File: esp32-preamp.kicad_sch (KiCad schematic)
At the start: 55 parts, among them J1 INPUT 1, J10 LFE, J11 OUT, J2 INPUT 2, J3 INPUT 3, J4 AMP PWR, J5 VOLUME, J6 TSOP382, J7 SELECT, J8 POT MOTOR, J9 PWR IN, Q1 2N3904, Q2 2N3904, Q3 2N3904, Q4 2N3904, U3 TSR0.5-2450, U4 TLV702475DBV, U5 TPS60402DBV, U6 ESP32 D1 Mini, U7 TPS72301DBV

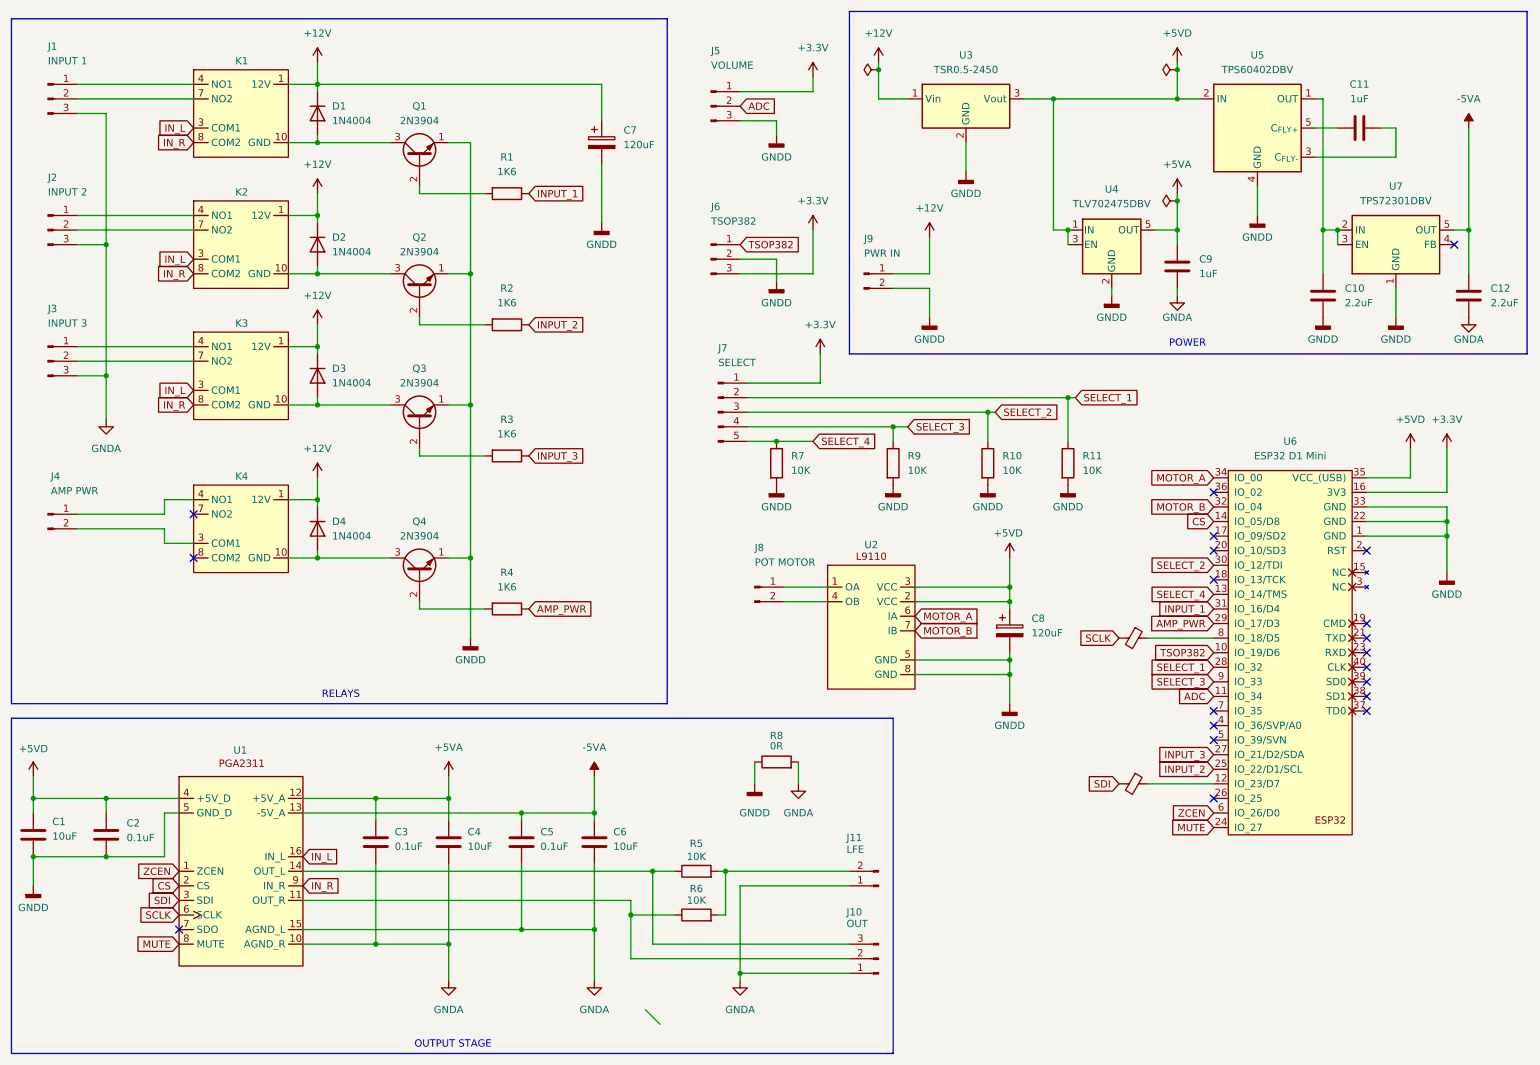
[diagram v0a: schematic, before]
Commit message: Fix J7 to reflect two input preamp
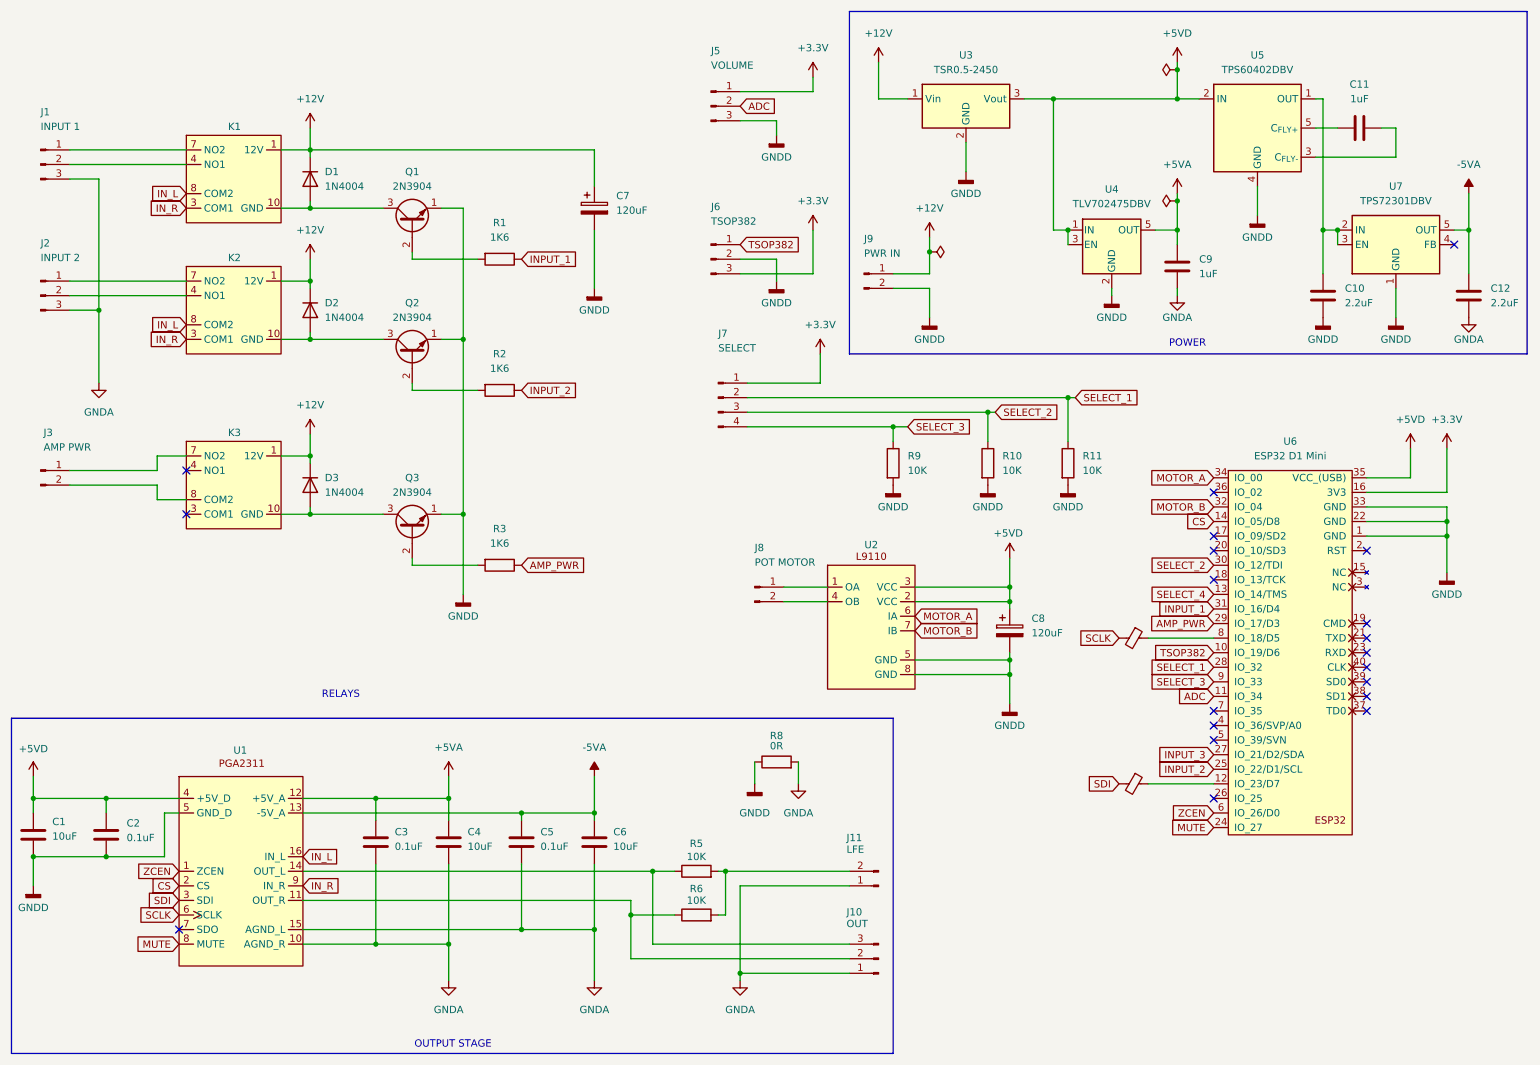
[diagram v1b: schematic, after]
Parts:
- removed D3: 1N4004, Diode_THT:D_DO-41_SOD81_P10.16mm_Horizontal, symbol Diode:1N4004
- removed J3: INPUT 3, Connector_JST:JST_XH_B3B-XH-A_1x03_P2.50mm_Vertical, symbol Connector:Conn_01x03_Pin
- removed J7: SELECT, Connector_JST:JST_XH_B5B-XH-A_1x05_P2.50mm_Vertical, symbol Connector:Conn_01x05_Pin
- removed K3: (no value), Panasonic TQ2:RELAY_TQ2_PAN, symbol Relay:TQ2
- removed Q3: 2N3904, Package_TO_SOT_THT:TO-92_Inline, symbol Transistor_BJT:2N3904
- removed R3: 1K6, Resistor_SMD:R_1206_3216Metric_Pad1.30x1.75mm_HandSolder, symbol Device:R
- removed R7: 10K, Resistor_SMD:R_1206_3216Metric_Pad1.30x1.75mm_HandSolder, symbol Device:R
- added J7: SELECT, Connector_JST:JST_XH_B4B-XH-A_1x04_P2.50mm_Vertical, symbol Connector:Conn_01x04_Pin
- C4: footprint Capacitor_SMD:C_1206_3216Metric_Pad1.33x1.80mm_HandSolder -> Capacitor_THT:C_Radial_D4.0mm_H5.0mm_P1.50mm
- R5, R6: footprint Resistor_THT:R_Axial_Power_L38.0mm_W9.0mm_P40.64mm -> Resistor_THT:R_Axial_Power_L30.0mm_W9.0mm_P36.4mm
- U4: footprint Package_TO_SOT_SMD:SOT-23-5_HandSoldering -> Package_TO_SOT_SMD:SOT-23-5
- U6: footprint ESP32 D1 Mini:esp32-wemos-d1-mini -> esp32-wemos-d1-mini:esp32-wemos-d1-mini
- renumbered D4 to D3, J4 to J3, K4 to K3, Q4 to Q3, R4 to R3
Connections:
- net +3.3V: now also J7.1 (Pin_1)
- net IN_L: now also K1.8 (COM2), K2.8 (COM2); no longer K1.3 (COM1), K2.3 (COM1)
- net IN_R: now also K1.3 (COM1), K2.3 (COM1); no longer K1.8 (COM2), K2.8 (COM2)
- net SELECT_1: now also J7.2 (Pin_2)
- net SELECT_2: now also J7.3 (Pin_3)
- net SELECT_3: now also J7.4 (Pin_4)
- net at K1.4 (NO1): now also J1.2 (Pin_2); no longer J1.1 (Pin_1)
- net at K1.7 (NO2): now also J1.1 (Pin_1); no longer J1.2 (Pin_2)
- net at J2.1 (Pin_1): now also K2.7 (NO2); no longer K2.4 (NO1)
- net at J2.2 (Pin_2): now also K2.4 (NO1); no longer K2.7 (NO2)
- net at J3.1 (Pin_1): now also K3.7 (NO2); no longer K3.4 (NO1)
- net at J3.2 (Pin_2): now also K3.8 (COM2); no longer K3.3 (COM1)
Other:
- moved on the sheet: C7, D1, D2, D3, J1, J2, J3, K1, K2, K3, Q1, Q2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

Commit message: PGA2311
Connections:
- net +5VD: no longer U4.3 (EN)
- net GNDA: now also J10.2 (Pin_2), J11.3 (Pin_3); no longer J10.1 (Pin_1), J11.1 (Pin_1)
- net at R5.1, U1.14 (OUT_L): now also J11.2 (Pin_2); no longer J11.3 (Pin_3)
- net at R5.2, R6.2: now also J10.1 (Pin_1); no longer J10.2 (Pin_2)
- net at R6.1, U1.11 (OUT_R): now also J11.1 (Pin_1); no longer J11.2 (Pin_2)
- no-connect marks 20 -> 21

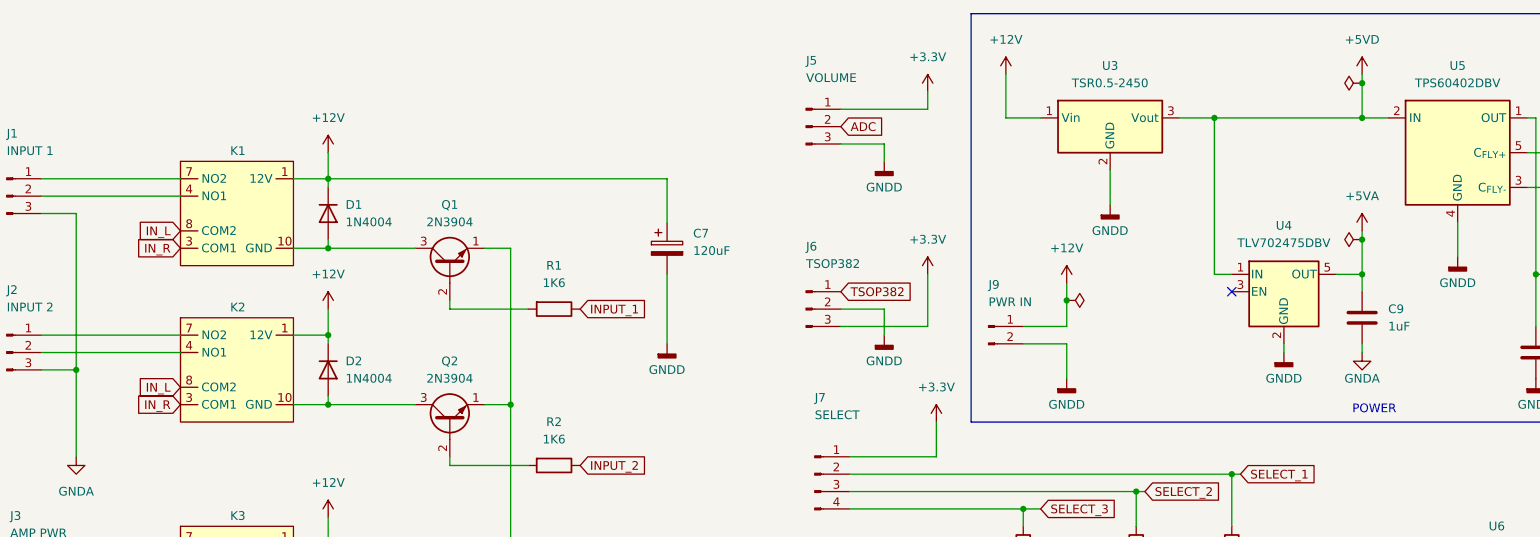
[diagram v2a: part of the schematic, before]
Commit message: More 5VA routing
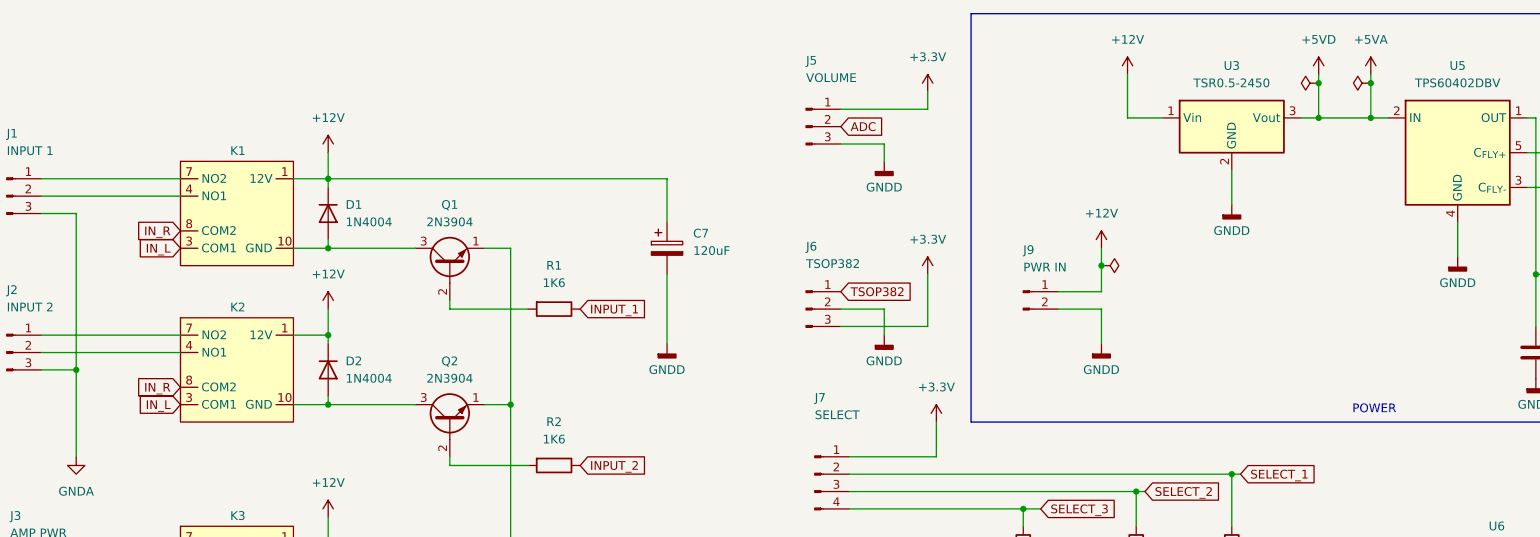
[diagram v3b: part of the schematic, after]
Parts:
- removed C9: 1uF, Capacitor_SMD:C_1206_3216Metric_Pad1.33x1.80mm_HandSolder, symbol Device:C
- removed U4: TLV702475DBV, Package_TO_SOT_SMD:SOT-23-5, symbol Regulator_Linear:TLV702475_SOT23-5
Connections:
- net +5VD is gone; now on net +5VA: C1.1, C2.1, C8.1, U1.4 (+5V_D), U2.2 (VCC), U2.3 (VCC), U3.3 (Vout), U5.2 (IN), U6.35 (VCC_(USB))
- net IN_L: now also K1.3 (COM1), K2.3 (COM1); no longer K1.8 (COM2), K2.8 (COM2)
- net IN_R: now also K1.8 (COM2), K2.8 (COM2); no longer K1.3 (COM1), K2.3 (COM1)
- no-connect marks 21 -> 20
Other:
- moved on the sheet: J9, U3
